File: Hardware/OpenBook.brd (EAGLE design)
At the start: 170.2 x 111.2 mm, 103 parts, among them IC1 XC6220A331MR-G, IC2 BD5229G-TR, J1 SAMACSYS_PARTS_USB4110-GF-A, J2 112A-TAAR-R03_ATTEND, J3 FH34SRJ-24S-0.5SH_99_, J4 QWIIC_RIGHT_ANGLE, Q1 20V/4.2A/52mΩ/1.4W, Q2 SI1308EDL-T1-GE3, Q3 20V/4.2A/52mΩ/1.4W, U1 BME688, U2 MCP73831, U3 ESP32-C6-WROOM-1-N8, U4 MAX17048G+T10, U5 DS3231SN#, U6 W25Q512JVEIQ

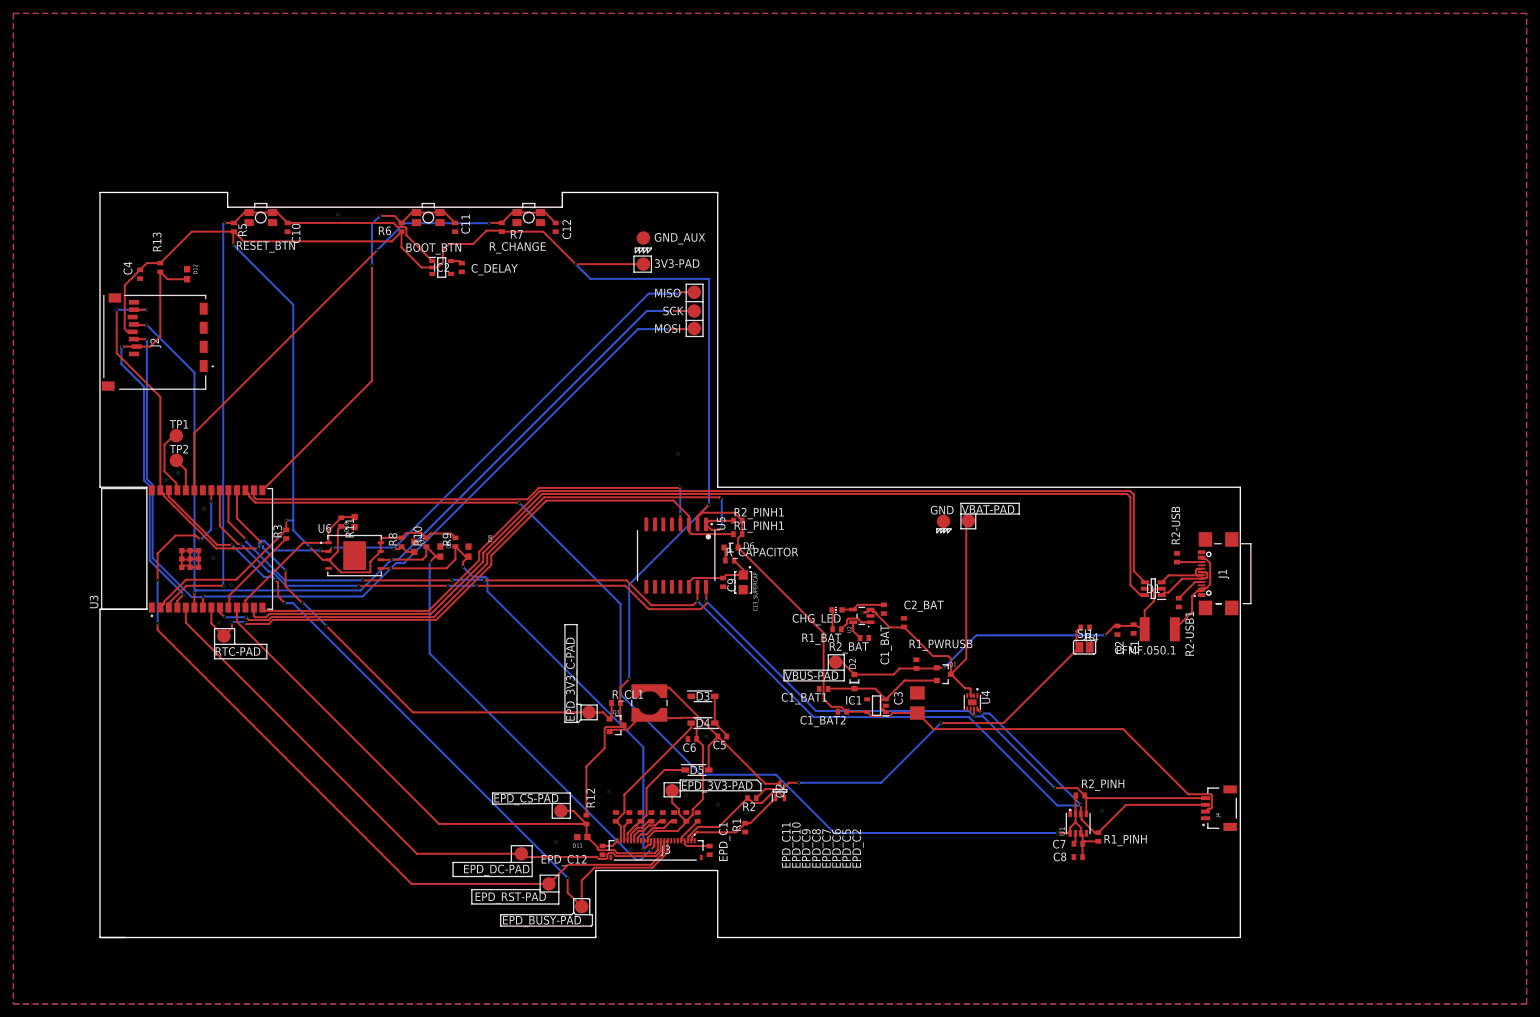
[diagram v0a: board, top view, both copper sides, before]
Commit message: Fixed some stuff
+Added via stitching around mcu
+Fixed inductor footprint with pads
+Added missing values to resistors
+Approved redundent erc warnings
+Fixed unconnected nets
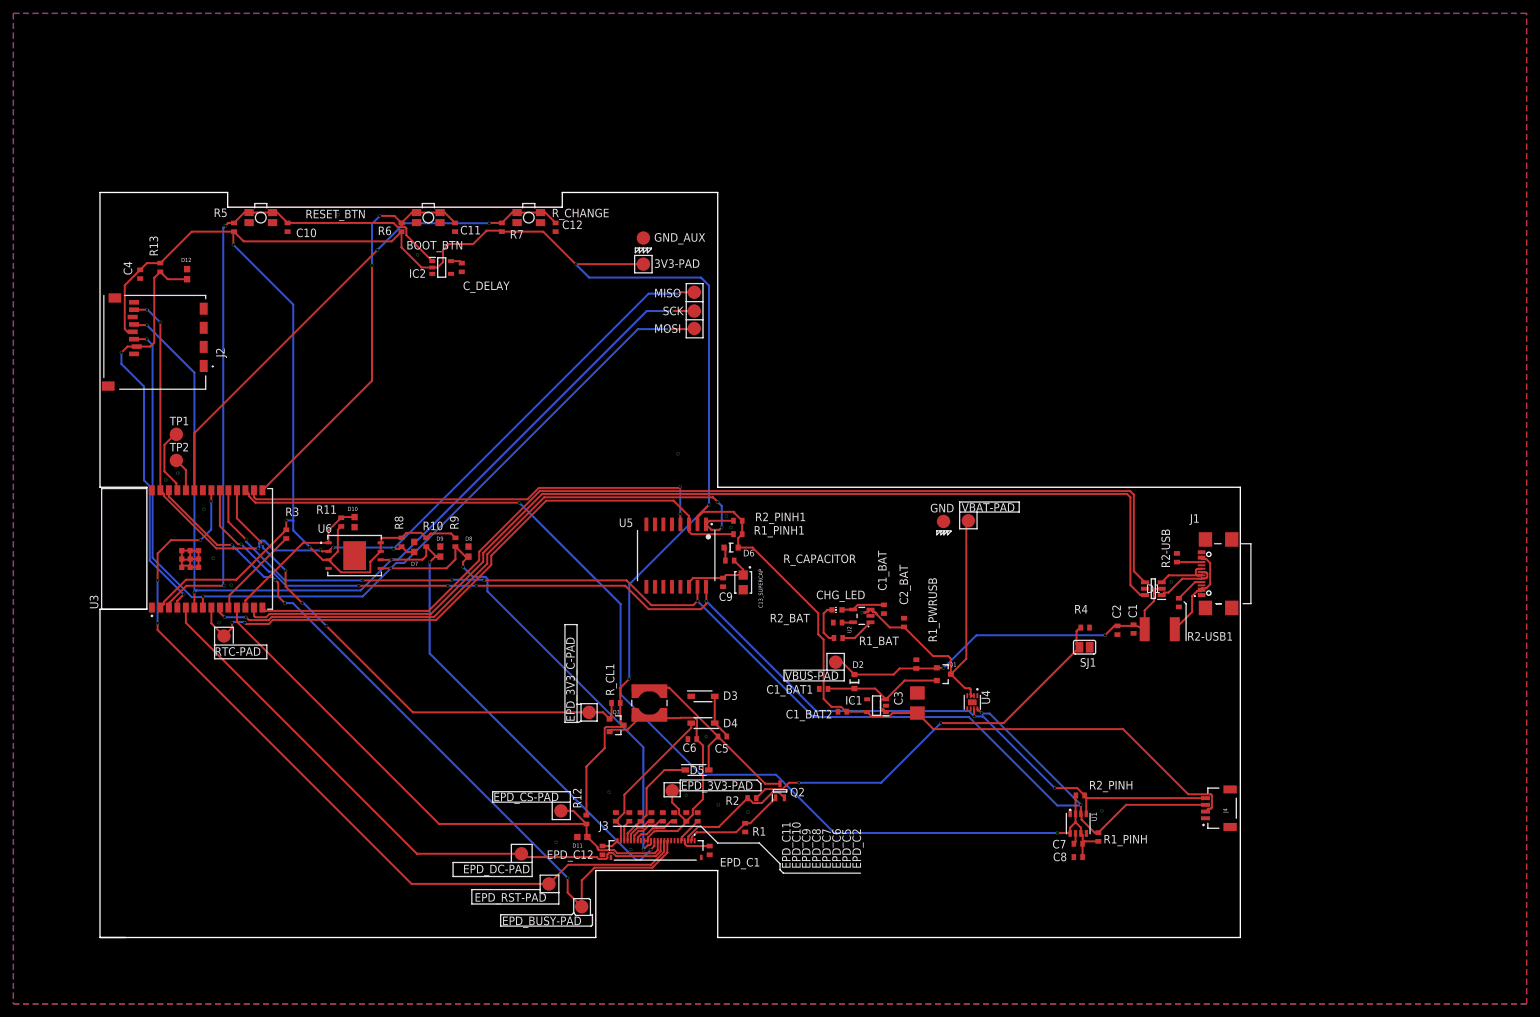
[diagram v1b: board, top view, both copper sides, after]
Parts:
- R5, R6, R7: value (none) -> 10K
- R_CAPACITOR: value (none) -> 15
- moved R2_BAT 4.61 mm to (110.1, 47.0), turned to 0 degrees
- moved R1_BAT 1.32 mm to (110.2, 44.7), turned to 0 degrees
- moved TP1 0.20 mm to (11.4, 75.1)
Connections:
- net N$12: now also U2.1; no longer CHG_LED.C
- net N$14: now also CHG_LED.C; no longer U2.1
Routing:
- net MISO: track 140.9 -> 134.6 mm
- net N$12: track 2.94 -> 5.12 mm
- net N$10: track 2.78 -> 1.67 mm
- net 3V3: track 433.2 -> 434.0 mm
- net N$14: track 5.57 -> 6.21 mm
- net 32KHZ: track 96.0 -> 95.4 mm
- net EPD_RST: track 122.3 -> 121.7 mm
- net GND: vias 18 -> 21
